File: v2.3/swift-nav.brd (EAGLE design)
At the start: 53 x 53 mm, 153 parts, among them J1 SMA_EDGE, J6 ZX62-B-5PA, Q1 IRLML6401, U1 6SLX9FTG256, U10 MAX2769, U12 PT7M8206B33TA5EX, U13 M25PX80, U2 LTC3407A_DFN, U3 STM32-M-64-LQFP, U4 7Q-16.368MBG-T, U5 SMA_PATCH_SMDGND, U6 93LC56BT-I/OT, U7 FT232HQ, U8 B4050, U9 XC2401, X3 FPGA DEBUG, X4 NX5032GA-12M, X5 CONN_5-2

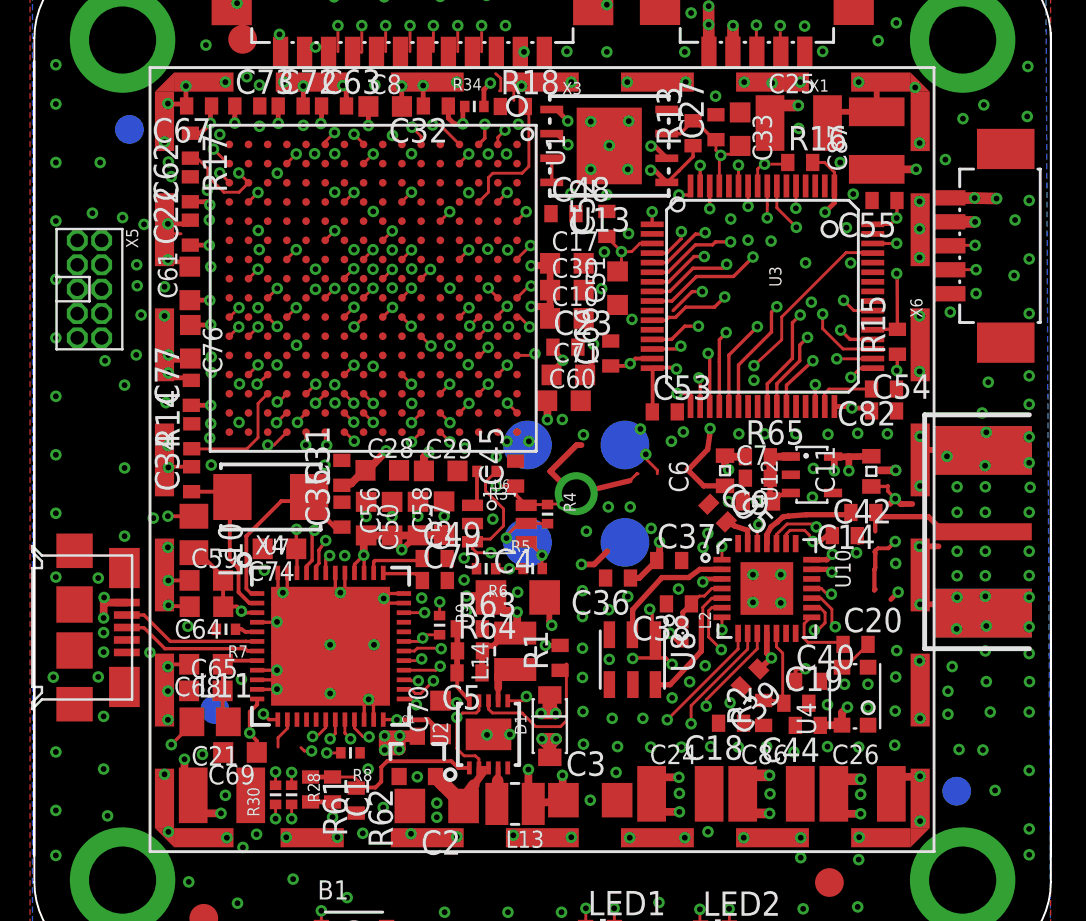
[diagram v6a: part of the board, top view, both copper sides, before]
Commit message: Removed fiducials from bottom of board
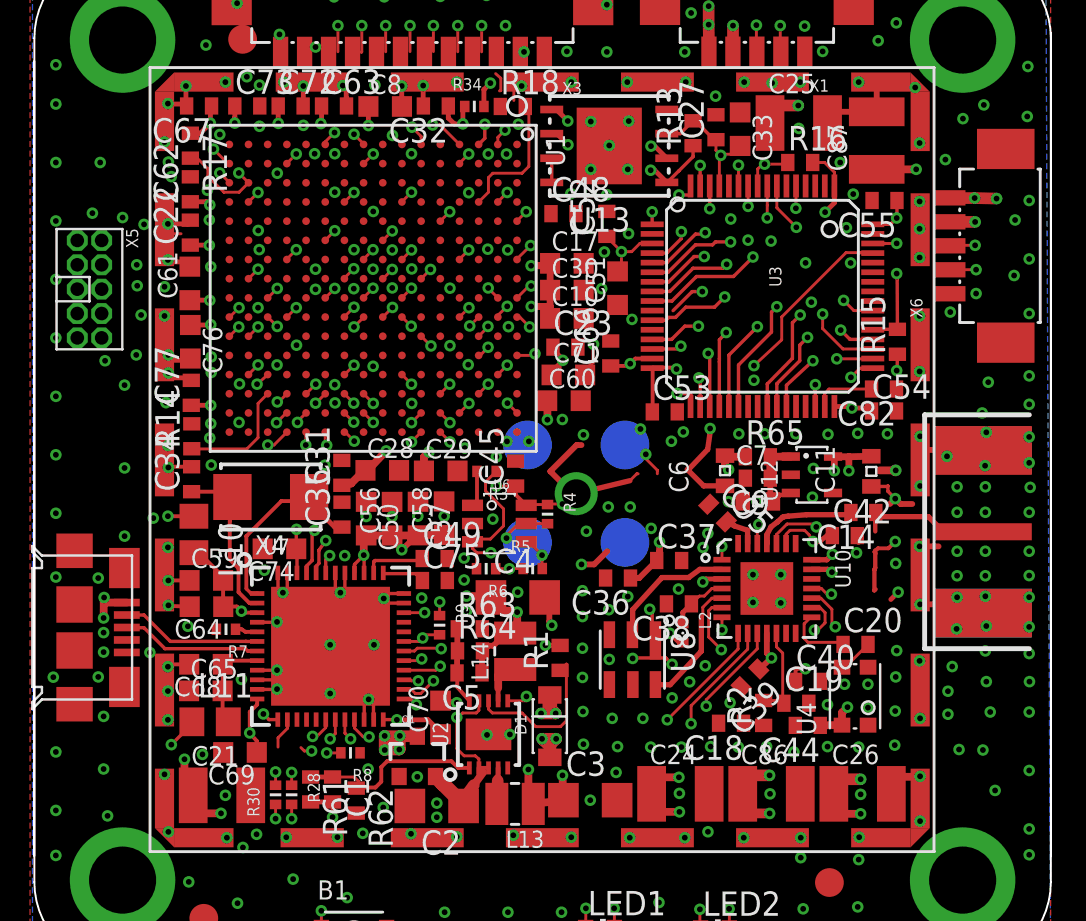
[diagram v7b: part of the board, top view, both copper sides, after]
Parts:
- removed JP5, JP6, JP7: FIDUCIAL1.5X3, aspirin:FIDUCIAL-1.5X3
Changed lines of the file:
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@@
 <grid distance="1" unitdist="mil" unit="mil" style="lines" multiple="1" display="yes" altdistance="0.25" altunitdist="mil" altunit="mil"/>
 <layers>
-<layer number="1" name="Top" color="4" fill="1" visible="yes" active="yes"/>
+<layer number="1" name="Top" color="4" fill="1" visible="no" active="yes"/>
 <layer number="2" name="Route2" color="1" fill="3" visible="no" active="yes"/>
 <layer number="3" name="Route3" color="4" fill="3" visible="no" active="yes"/>
@@
 <layer number="14" name="Route14" color="1" fill="6" visible="no" active="yes"/>
 <layer number="15" name="Route15" color="4" fill="6" visible="no" active="yes"/>
-<layer number="16" name="Bottom" color="1" fill="1" visible="no" active="yes"/>
+<layer number="16" name="Bottom" color="1" fill="1" visible="yes" active="yes"/>
 <layer number="17" name="Pads" color="2" fill="1" visible="yes" active="yes"/>
 <layer number="18" name="Vias" color="2" fill="1" visible="yes" active="yes"/>
 <layer number="19" name="Unrouted" color="6" fill="1" visible="yes" active="yes"/>
 <layer number="20" name="Dimension" color="15" fill="1" visible="yes" active="yes"/>
-<layer number="21" name="tPlace" color="7" fill="1" visible="yes" active="yes"/>
-<layer number="22" name="bPlace" color="7" fill="1" visible="no" active="yes"/>
-<layer number="23" name="tOrigins" color="15" fill="1" visible="yes" active="yes"/>
-<layer number="24" name="bOrigins" color="15" fill="1" visible="no" active="yes"/>
+<layer number="21" name="tPlace" color="7" fill="1" visible="no" active="yes"/>
+<layer number="22" name="bPlace" color="7" fill="1" visible="yes" active="yes"/>
+<layer number="23" name="tOrigins" color="15" fill="1" visible="no" active="yes"/>
+<layer number="24" name="bOrigins" color="15" fill="1" visible="yes" active="yes"/>
 <layer number="25" name="tNames" color="7" fill="1" visible="no" active="yes"/>
 <layer number="26" name="bNames" color="7" fill="1" visible="no" active="yes"/>
@@
 <element name="R28" library="pel_dipol_comp" package="0402-RES" value="150" x="16.8148" y="12.446" rot="R270"/>
 <element name="R30" library="pel_dipol_comp" package="0402-RES" value="150" x="15.9766" y="12.446" rot="R90"/>
-<element name="JP5" library="aspirin" package="FIDUCIAL-1.5X3" value="FIDUCIAL1.5X3" x="51.4898" y="12.634" rot="MR180"/>
-<element name="JP6" library="aspirin" package="FIDUCIAL-1.5X3" value="FIDUCIAL1.5X3" x="8.3586" y="47.138" rot="MR270"/>
-<element name="JP7" library="aspirin" package="FIDUCIAL-1.5X3" value="FIDUCIAL1.5X3" x="12.8128" y="16.8932" rot="MR270"/>
 <element name="JP8" library="aspirin" package="FIDUCIAL-1.5X3" value="FIDUCIAL1.5X3" x="44.854" y="7.873" rot="R90"/>
 <element name="JP9" library="aspirin" package="FIDUCIAL-1.5X3" value="FIDUCIAL1.5X3" x="14.2586" y="51.838" rot="R90"/>

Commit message: Debug connector was connected to VDD instead of V+ (post instead of pre-reverse polarity protection)
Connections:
- net V+: now also X3.12
- net VDD: no longer X3.12
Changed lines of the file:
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@@
 <grid distance="1" unitdist="mil" unit="mil" style="lines" multiple="1" display="yes" altdistance="0.25" altunitdist="mil" altunit="mil"/>
 <layers>
-<layer number="1" name="Top" color="4" fill="1" visible="no" active="yes"/>
+<layer number="1" name="Top" color="4" fill="1" visible="yes" active="yes"/>
 <layer number="2" name="Route2" color="1" fill="3" visible="no" active="yes"/>
 <layer number="3" name="Route3" color="4" fill="3" visible="no" active="yes"/>
@@
 <layer number="14" name="Route14" color="1" fill="6" visible="no" active="yes"/>
 <layer number="15" name="Route15" color="4" fill="6" visible="no" active="yes"/>
-<layer number="16" name="Bottom" color="1" fill="1" visible="yes" active="yes"/>
+<layer number="16" name="Bottom" color="1" fill="1" visible="no" active="yes"/>
 <layer number="17" name="Pads" color="2" fill="1" visible="yes" active="yes"/>
 <layer number="18" name="Vias" color="2" fill="1" visible="yes" active="yes"/>
 <layer number="19" name="Unrouted" color="6" fill="1" visible="yes" active="yes"/>
 <layer number="20" name="Dimension" color="15" fill="1" visible="yes" active="yes"/>
-<layer number="21" name="tPlace" color="7" fill="1" visible="no" active="yes"/>
-<layer number="22" name="bPlace" color="7" fill="1" visible="yes" active="yes"/>
-<layer number="23" name="tOrigins" color="15" fill="1" visible="no" active="yes"/>
-<layer number="24" name="bOrigins" color="15" fill="1" visible="yes" active="yes"/>
+<layer number="21" name="tPlace" color="7" fill="1" visible="yes" active="yes"/>
+<layer number="22" name="bPlace" color="7" fill="1" visible="no" active="yes"/>
+<layer number="23" name="tOrigins" color="15" fill="1" visible="yes" active="yes"/>
+<layer number="24" name="bOrigins" color="15" fill="1" visible="no" active="yes"/>
 <layer number="25" name="tNames" color="7" fill="1" visible="no" active="yes"/>
 <layer number="26" name="bNames" color="7" fill="1" visible="no" active="yes"/>
@@
 <wire x1="48.9331" y1="44.2722" x2="51.7144" y2="44.2722" width="0.6096" layer="15"/>
 <wire x1="51.7144" y1="44.2722" x2="52.4256" y2="43.561" width="0.6096" layer="15"/>
+<contactref element="X3" pad="12"/>
+<wire x1="38.5718" y1="51.1832" x2="16.239" y2="51.1732" width="0" layer="19" extent="1-1"/>
 </signal>
 <signal name="SPI2NSS_FPGA">
@@
 <wire x1="31.6526" y1="28.1474" x2="-12.85" y2="-9.6" width="0" layer="19" extent="1-1"/>
 </signal>
-<signal name="N$1">
-</signal>
 <signal name="N$23">
 <contactref element="U6" pad="5"/>
@@
 <via x="39.5986" y="29.4005" extent="1-16" drill="0.3"/>
 <wire x1="39.5986" y1="29.4005" x2="39.5986" y2="29.0576" width="0.4064" layer="3"/>
-<contactref element="X3" pad="12"/>
-<wire x1="33.401" y1="31.1658" x2="16.239" y2="51.1732" width="0" layer="19" extent="1-3"/>
 </signal>
 <signal name="N$18">
